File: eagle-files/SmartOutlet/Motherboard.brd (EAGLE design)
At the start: 58.4 x 68.2 mm, 35 parts, among them IC1 1117, T1 CST-1025, U1 ADS1115IDGST, U2 ESP-WROOM-32, U3 FT232RL, X1 22-23-2041, X2 22-23-2021

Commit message: Updated eagle files
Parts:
- removed LED4, LED5, LED6: (no value), adafruit:CHIP-LED0603
- removed T1: CST-1025, CST-1025:XFMR_CST-1025
- removed X1: 22-23-2041, con-molex:22-23-2041
- added CURRENT_TRANSFORMER: CST-1025, CST-1025:XFMR_CST-1025
- added POWER_LED, RX_LED, TX_LED: (no value), adafruit:CHIP-LED0603
- added U$1: MICRO-USB, microusb:MICRO-USB
- U1: value ADS1115IDGST -> ADS1115
- moved R3 20.5 mm to (22.9, 40.6), turned to 0 degrees
- moved FB1 17.3 mm to (21.6, 34.3)
- moved C2 15.9 mm to (22.9, 30.5), turned to 0 degrees
- moved C1 15.9 mm to (22.9, 38.1), turned to 180 degrees
- moved R1 15.9 mm to (22.9, 43.2), turned to 0 degrees
- moved R4 15.9 mm to (22.9, 48.3)
- moved FB2 14.9 mm to (24.1, 34.3)
- moved LED1 14.6 mm to (29.8, 26.0), turned to 180 degrees
- moved R9 13.7 mm to (36.8, 11.4)
- moved R10 13.7 mm to (36.8, 16.5)
- moved R7 13.7 mm to (36.8, 6.35)
- moved C19 12.6 mm to (2.54, 22.9), turned to 90 degrees
- moved R2 11.7 mm to (22.9, 45.7), turned to 0 degrees
- moved R6 11.4 mm to (40.6, 22.9), turned to 180 degrees
- moved S2 11.4 mm to (40.6, 27.9)
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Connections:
- net +5V: now also U$1.1, X2.1; no longer X1.1, X2.2
- net BLUE: now also R16.1; no longer R17.1
- net DIFF_INPUT_1: now also CURRENT_TRANSFORMER.1; no longer T1.1
- net DIFF_INPUT_2: now also CURRENT_TRANSFORMER.2; no longer T1.2
- net GND: now also POWER_LED.C, U$1.5, U$1.GND1, U$1.GND2, X2.2; no longer LED6.C, X1.4, X2.1
- net GREEN: now also R17.1; no longer R16.1
- net N$13: now also RX_LED.A; no longer LED5.A
- net N$3: now also TX_LED.A; no longer LED4.A
- net PLUG_D+: now also U$1.3; no longer X1.3
- net PLUG_D-: now also U$1.2; no longer X1.2
- net POWER_LED: now also POWER_LED.A; no longer LED6.A
- net RX_LED: now also RX_LED.C; no longer LED5.C
- net TX_LED: now also TX_LED.C; no longer LED4.C
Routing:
- net GND: track 0.00 -> 166.0 mm, vias 0 -> 2
- net +5V: track 0.00 -> 107.3 mm, vias 0 -> 4
- net RTS: track 0.00 -> 101.5 mm, vias 0 -> 2
- net 3.3V: track 0.00 -> 90.7 mm, vias 0 -> 5
- net DTR: track 0.00 -> 58.0 mm, vias 0 -> 2
- net TX_MCU: track 0.00 -> 54.4 mm, vias 0 -> 2
- net RX_MCU: track 0.00 -> 50.9 mm, vias 0 -> 2
- net SCL: track 0.00 -> 38.2 mm, vias 0 -> 2
- net SDA: track 0.00 -> 34.3 mm, vias 0 -> 2
- net DIFF_INPUT_2: track 0.00 -> 32.4 mm
- net BUTTON: track 0.00 -> 28.1 mm, vias 0 -> 1
- net ADC_GND: track 0.00 -> 22.5 mm, vias 0 -> 2
- net ADC_VCC: track 0.00 -> 22.4 mm
- net ADDR: track 0.00 -> 19.0 mm, vias 0 -> 2
- net 3V3: track 0.00 -> 18.1 mm
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- added copper zone on layer 1, net GND
- added copper zone on layer 16, net GND
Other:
- board size 58.4 x 68.2 mm -> 50.8 x 60.6 mm

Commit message: Updated eagle files
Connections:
- net BUTTON: now also U2.29; no longer U2.27
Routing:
- net BUTTON: track 28.1 -> 30.6 mm
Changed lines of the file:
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@@
 <signal name="BUTTON">
 <contactref element="R6" pad="1"/>
-<contactref element="U2" pad="27"/>
 <contactref element="S2" pad="3"/>
 <wire x1="41.49" y1="22.86" x2="41.49" y2="24.13" width="0.254" layer="1"/>
@@
 <wire x1="39.6494" y1="27.94" x2="44.45" y2="27.94" width="0.254" layer="16"/>
 <wire x1="44.45" y1="27.94" x2="45.974" y2="29.464" width="0.254" layer="16"/>
-<via x="45.974" y="38.735" extent="1-16" drill="0.35"/>
-<wire x1="45.974" y1="38.735" x2="48.605" y2="38.735" width="0.254" layer="1"/>
-<wire x1="48.605" y1="38.735" x2="48.62" y2="38.75" width="0.254" layer="1"/>
-<wire x1="45.974" y1="29.464" x2="45.974" y2="38.735" width="0.254" layer="16"/>
+<via x="45.974" y="41.275" extent="1-16" drill="0.35"/>
+<wire x1="45.974" y1="29.464" x2="45.974" y2="41.275" width="0.254" layer="16"/>
+<contactref element="U2" pad="29"/>
+<wire x1="45.974" y1="41.275" x2="48.605" y2="41.275" width="0.254" layer="1"/>
+<wire x1="48.605" y1="41.275" x2="48.62" y2="41.29" width="0.254" layer="1"/>
 </signal>
 <signal name="3.3V">

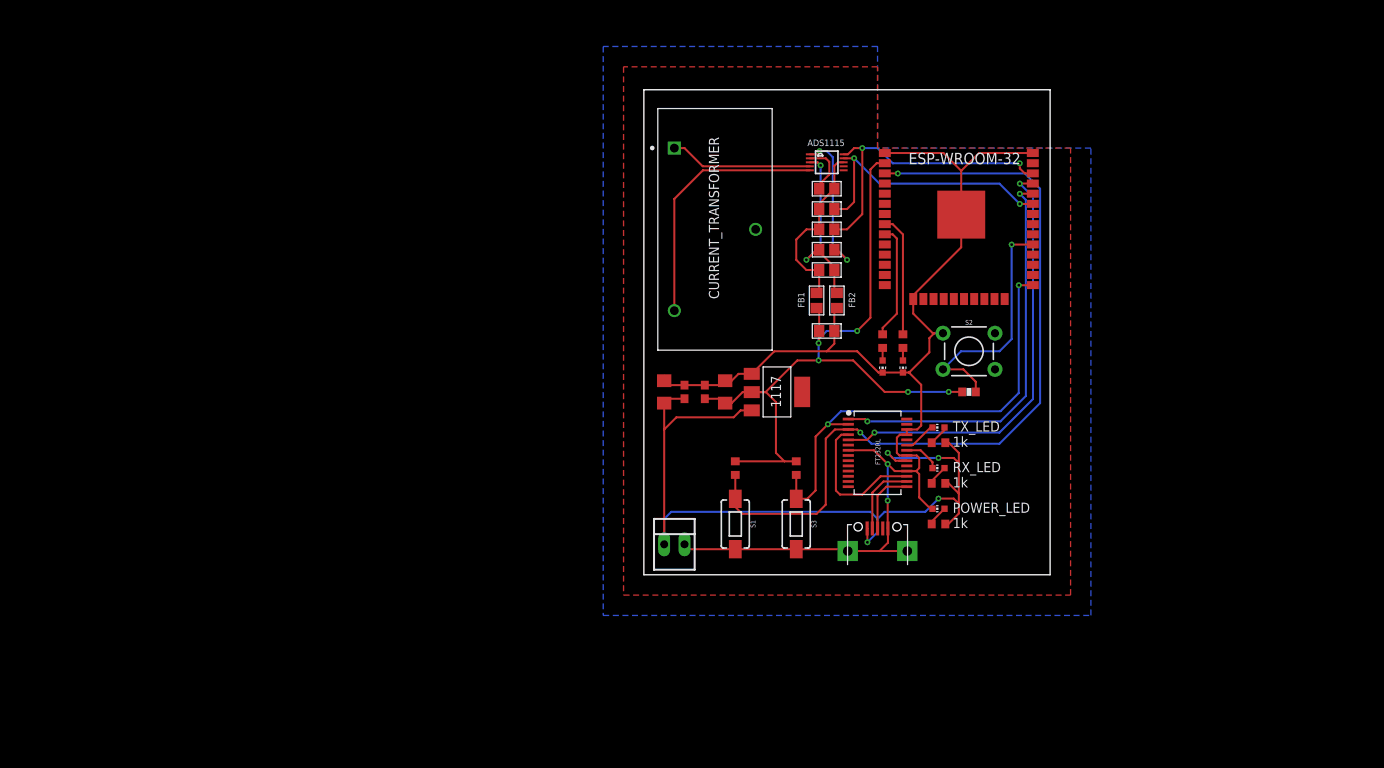
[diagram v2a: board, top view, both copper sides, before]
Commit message: Added daughter board and edited motherboard
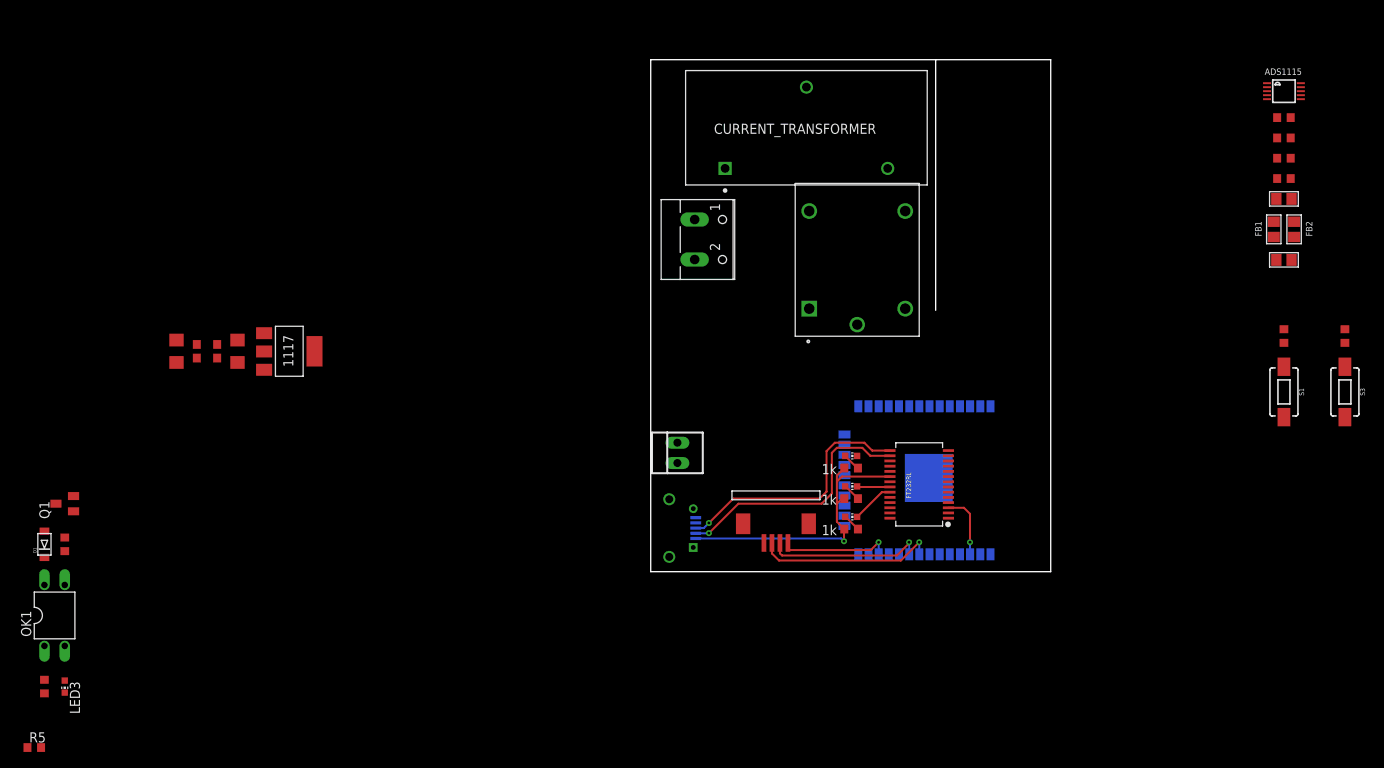
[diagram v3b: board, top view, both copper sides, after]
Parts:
- removed LED1, LED2: (no value), adafruit:CHIP-LED0603
- removed R6: 10k, rcl:R0603
- removed S2: MOMENTARY-SWITCH-SPST-PTH-6.0MM, SparkFun-Switches:TACTILE_SWITCH_PTH_6.0MM
- removed U$1: MICRO-USB, microusb:MICRO-USB
- added D1: (no value), adafruit:SOD-123FL
- added K1: SRD-05VDC-SL-C, SRD-05VDC-SL-C:RELAY_SRD-05VDC-SL-C
- added K2: 68610414122, 4_pin_smd_connector:68610414122
- added LED3: (no value), adafruit_custom:CHIP-LED0603
- added OK1: PC817, optocoupler:DIL04
- added Q1: (no value), semicon-smd-ipc:SOT23
- added R5: 1k, rcl:R0603
- added U$2: ZX62D-B-5P8, j_usb_hirose_zx62d-b-5p8:ZX62D-B-5P8
- added X1: (no value), con-wago-500:W237-102
- C20, C21: value 100nF -> 0.1uF
- POWER_LED, RX_LED, TX_LED: device adafruit:CHIP-LED0603 -> adafruit_custom:CHIP-LED0603
- R1, R2, R3, R4: device microbuilder:0805 -> rcl:R0603
- R10, R11, R7, R8, R9: device eagle-ltspice:R0603 -> rcl:R0603
- R16: value 1k -> 510; device adafruit:R0603 -> rcl:R0603
- R17: device adafruit:R0603 -> rcl:R0603
- moved R17 113.3 mm to (-74.9, -14.0)
- moved R16 107.8 mm to (-72.4, 3.81), turned to 90 degrees
- moved R8 70.5 mm to (80.0, 29.8)
- moved S1 70.5 mm to (80.0, 22.9)
- moved R11 70.5 mm to (87.6, 29.8)
- moved S3 70.5 mm to (87.6, 22.9)
- moved C19 61.2 mm to (-58.4, 27.9)
- moved C20 61.2 mm to (-53.3, 27.9)
- moved C21 61.2 mm to (-55.9, 27.9)
- moved IC1 61.2 mm to (-44.3, 27.9)
- moved C18 61.2 mm to (-50.8, 27.9)
- moved C1 57.8 mm to (80.0, 47.0)
- moved C2 57.8 mm to (80.0, 39.4)
- moved FB2 57.8 mm to (81.3, 43.2)
- moved R1 57.8 mm to (80.0, 52.1)
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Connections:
- removed net N$5: LED1.A, R17.2
- removed net N$6: LED2.A, R16.2
- new net N$1: LED3.A, OK1.2
- new net N$2: OK1.1, R17.1
- new net N$4: OK1.3, R16.1
- new net N$7: Q1.1, R16.2
- new net N$8: D1.A, K1.A2, Q1.3
- new net POWER_IN: K1.COM, X1.2
- new net POWER_SWITCHED: K1.NC, X1.1
- new net RELAY: LED3.C, U2.28
- net +5V: now also D1.C, K1.A1, OK1.4, U$2.P$1, X2.2; no longer U$1.1, X2.1
- net 3.3V: now also R17.2, R5.1; no longer R6.2
- net BLUE: now also K2.3; no longer R16.1
- net BUTTON: now also K2.1, R5.2, U2.12; no longer R6.1, S2.3, U2.29
- net GND: now also K2.4, Q1.2, U$2.P$5, X2.1; no longer LED1.C, LED2.C, S2.1, U$1.5, U$1.GND1, U$1.GND2, X2.2
- net GREEN: now also K2.2; no longer R17.1
- net PLUG_D+: now also U$2.P$3; no longer U$1.3
- net PLUG_D-: now also U$2.P$2; no longer U$1.2
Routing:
- net GND: track 166.0 -> 0.00 mm, vias 2 -> 0
- net RTS: track 101.5 -> 8.07 mm, vias 2 -> 1
- net 3.3V: track 90.7 -> 0.00 mm, vias 5 -> 0
- net +5V: track 107.3 -> 36.7 mm, vias 4 -> 1
- net DTR: track 58.0 -> 0.00 mm, vias 2 -> 0
- net TX_MCU: track 54.4 -> 0.00 mm, vias 2 -> 0
- net RX_MCU: track 50.9 -> 0.00 mm, vias 2 -> 0
- net SCL: track 38.2 -> 0.00 mm, vias 2 -> 0
- net SDA: track 34.3 -> 0.00 mm, vias 2 -> 0
- net DIFF_INPUT_2: track 32.4 -> 0.00 mm
- net PLUG_D+: track 8.23 -> 32.1 mm, vias 0 -> 1
- net PLUG_D-: track 9.36 -> 32.1 mm, vias 0 -> 1
- net ADC_GND: track 22.5 -> 0.00 mm, vias 2 -> 0
- net ADC_VCC: track 22.4 -> 0.00 mm
- net ADDR: track 19.0 -> 0.00 mm, vias 2 -> 0
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- removed copper zone on layer 1, net GND
- removed copper zone on layer 16, net GND
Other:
- board size 50.8 x 60.6 mm -> 50 x 64 mm

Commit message: Updated PCB design
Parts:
- removed CURRENT_TRANSFORMER: CST-1025, CST-1025:XFMR_CST-1025
- removed LED3: (no value), adafruit_custom:CHIP-LED0603
- removed S3: MOMENTARY-SWITCH-SPST-SMD-6.0X3.5MM, SparkFun-Switches:TACTILE_SWITCH_SMD_6.0X3.5MM
- added C3: 0.1uF, SparkFun-Capacitors:0603
- added C4: 1nF, SparkFun-Capacitors:0603
- added RELAY: (no value), adafruit_custom:CHIP-LED0603
- added S2: TL1015AF160QG, small_tactile_switch:SW_TL1015AF160QG
- added U4: ACS712ELCTR-20A-T, ACS712ELCTR-20A-T:SOIC127P600X175-8N
- S1: value MOMENTARY-SWITCH-SPST-SMD-6.0X3.5MM -> TL1015AF160QG; device SparkFun-Switches:TACTILE_SWITCH_SMD_6.0X3.5MM -> small_tactile_switch:SW_TL1015AF160QG
- moved R17 122.4 mm to (31.8, 46.1), turned to 180 degrees
- moved OK1 116.9 mm to (29.2, 50.5), turned to 90 degrees
- moved R16 114.5 mm to (29.2, 56.5)
- moved Q1 114.3 mm to (29.2, 61.2)
- moved D1 113.3 mm to (25.4, 56.5)
- moved R5 96.3 mm to (10.2, 21.0), turned to 90 degrees
- moved C19 88.3 mm to (29.8, 31.1), flipped to the bottom
- moved C21 83.2 mm to (27.3, 31.1), flipped to the bottom
- moved C20 78.2 mm to (24.8, 31.1), flipped to the bottom
- moved C18 73.1 mm to (22.2, 31.1), flipped to the bottom
- moved R11 71.2 mm to (16.5, 26.7), turned to 0 degrees
- moved R8 63.5 mm to (16.5, 30.5), turned to 0 degrees
- moved S1 63.5 mm to (16.5, 22.9), turned to 180 degrees
- moved IC1 59.8 mm to (15.4, 31.1), flipped to the bottom
- moved U1 57.1 mm to (26.4, 40.8)
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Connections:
- net N$8 renamed RELAY_GND
- removed net DIFF_INPUT_1: CURRENT_TRANSFORMER.1, U1.4
- removed net DIFF_INPUT_2: CURRENT_TRANSFORMER.2, U1.5
- new net ACS_FILTER: C4.1, U4.6
- new net CURRENT_SENSOR: U1.4, U4.7
- new net POWER_OUT: U4.3, U4.4, X1.2
- net +5V: now also C2.1, C3.1, FB1.1, U4.8, X2.1; no longer X2.2
- net 3.3V: no longer C2.1, FB1.1
- net BLUE: now also K2.2, U2.9; no longer K2.3, U2.8
- net BUTTON: now also K2.3, U2.11; no longer K2.1, U2.12
- net DTR: now also S1.1; no longer S3.1
- net GND: now also C3.2, C4.2, S2.2, U4.5, X2.2; no longer S3.2, X2.1
- net GREEN: now also K2.1, U2.8; no longer K2.2, U2.9
- net N$1: now also RELAY.A; no longer LED3.A
- net POWER_IN: now also K1.NC, X1.1; no longer K1.COM, X1.2
- net POWER_SWITCHED: now also K1.COM, U4.1, U4.2; no longer K1.NC, X1.1
- net RELAY: now also RELAY.C; no longer LED3.C
- net RTS: now also S2.1; no longer S1.1
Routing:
- net GND: track 0.00 -> 206.0 mm, vias 0 -> 7
- net 3.3V: track 0.00 -> 113.4 mm, vias 0 -> 5
- net +5V: track 36.7 -> 143.3 mm, vias 1 -> 5
- net RTS: track 8.07 -> 50.8 mm
- net DTR: track 0.00 -> 38.5 mm, vias 0 -> 2
- net SCL: track 0.00 -> 34.4 mm, vias 0 -> 1
- net SDA: track 0.00 -> 33.7 mm, vias 0 -> 1
- net RELAY: track 0.00 -> 31.1 mm, vias 0 -> 3
- net POWER_SWITCHED: track 0.00 -> 23.7 mm
- net BUTTON: track 14.0 -> 33.9 mm
- net RX_MCU: track 0.00 -> 19.5 mm, vias 0 -> 1
- net ADC_VCC: track 0.00 -> 18.6 mm
- net POWER_OUT: track 0.00 -> 15.4 mm
- net RELAY_GND: track 0.00 -> 14.8 mm
- net ADC_GND: track 0.00 -> 14.6 mm
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- added copper zone on layer 1, net GND
- added copper zone on layer 16, net GND
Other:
- board size 50 x 64 mm -> 37.3 x 64 mm
- board text added: "+"
- board text added: "-"
- board text added: "ACS712"
- board text added: "Antenna"
- board text added: "BOOT"
- board text added: "Daughter Board"
- board text added: "EN"
- board text added: "In"
- board text added: "MICRO USB"
- board text added: "Out"
- board text added: "Power"
- board text added: "Relay"
- board text added: "Rx"
- board text added: "Tx"

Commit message: Updated eagle files
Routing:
- net +5V: track 143.3 -> 144.8 mm
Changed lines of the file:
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@@
 <drawing>
 <settings>
-<setting alwaysvectorfont="yes"/>
+<setting alwaysvectorfont="no"/>
 <setting verticaltext="up"/>
 </settings>
@@
 <wire x1="17.969" y1="43.561" x2="20.066" y2="43.561" width="0.6096" layer="1"/>
 <via x="20.066" y="43.561" extent="1-16" drill="0.35"/>
-<wire x1="20.066" y1="43.561" x2="16.51" y2="40.005" width="0.6096" layer="16"/>
-<wire x1="16.51" y1="40.005" x2="16.51" y2="29.21" width="0.6096" layer="16"/>
-<wire x1="16.51" y1="29.21" x2="16.9164" y2="28.8036" width="0.6096" layer="16"/>
+<wire x1="20.066" y1="43.561" x2="15.494" y2="38.989" width="0.6096" layer="16"/>
+<wire x1="15.494" y1="38.989" x2="15.494" y2="30.226" width="0.6096" layer="16"/>
+<wire x1="15.494" y1="30.226" x2="16.9164" y2="28.8036" width="0.6096" layer="16"/>
 <wire x1="16.9164" y1="28.8036" x2="19.05" y2="28.8036" width="0.6096" layer="16"/>
 <wire x1="4.191" y1="13.97" x2="4.953" y2="13.97" width="0.254" layer="1"/>
@@
 <wire x1="33.97" y1="28.194" x2="33.97" y2="28.702" width="0.254" layer="1"/>
 <wire x1="4.191" y1="13.97" x2="5.08" y2="13.97" width="0.254" layer="1"/>
-<wire x1="16.51" y1="29.21" x2="16.51" y2="27.559" width="0.6096" layer="16"/>
+<wire x1="15.494" y1="30.226" x2="15.494" y2="26.543" width="0.6096" layer="16"/>
 <wire x1="8.636" y1="19.685" x2="8.636" y2="18.161" width="0.6096" layer="16"/>
 <via x="8.636" y="18.161" extent="1-16" drill="0.35"/>
@@
 <wire x1="8.636" y1="17.78" x2="4.826" y2="13.97" width="0.6096" layer="1"/>
 <wire x1="4.826" y1="13.97" x2="4.191" y2="13.97" width="0.6096" layer="1"/>
-<wire x1="16.51" y1="27.559" x2="8.636" y2="19.685" width="0.6096" layer="16"/>
+<wire x1="15.494" y1="26.543" x2="8.636" y2="19.685" width="0.6096" layer="16"/>
 </signal>
 <signal name="3V3">
